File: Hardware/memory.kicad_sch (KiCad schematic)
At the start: 56 parts, among them J2 Micro_SD_Card_Det, U1 STM32MP157FAD1, U3 MT41K256M16TW

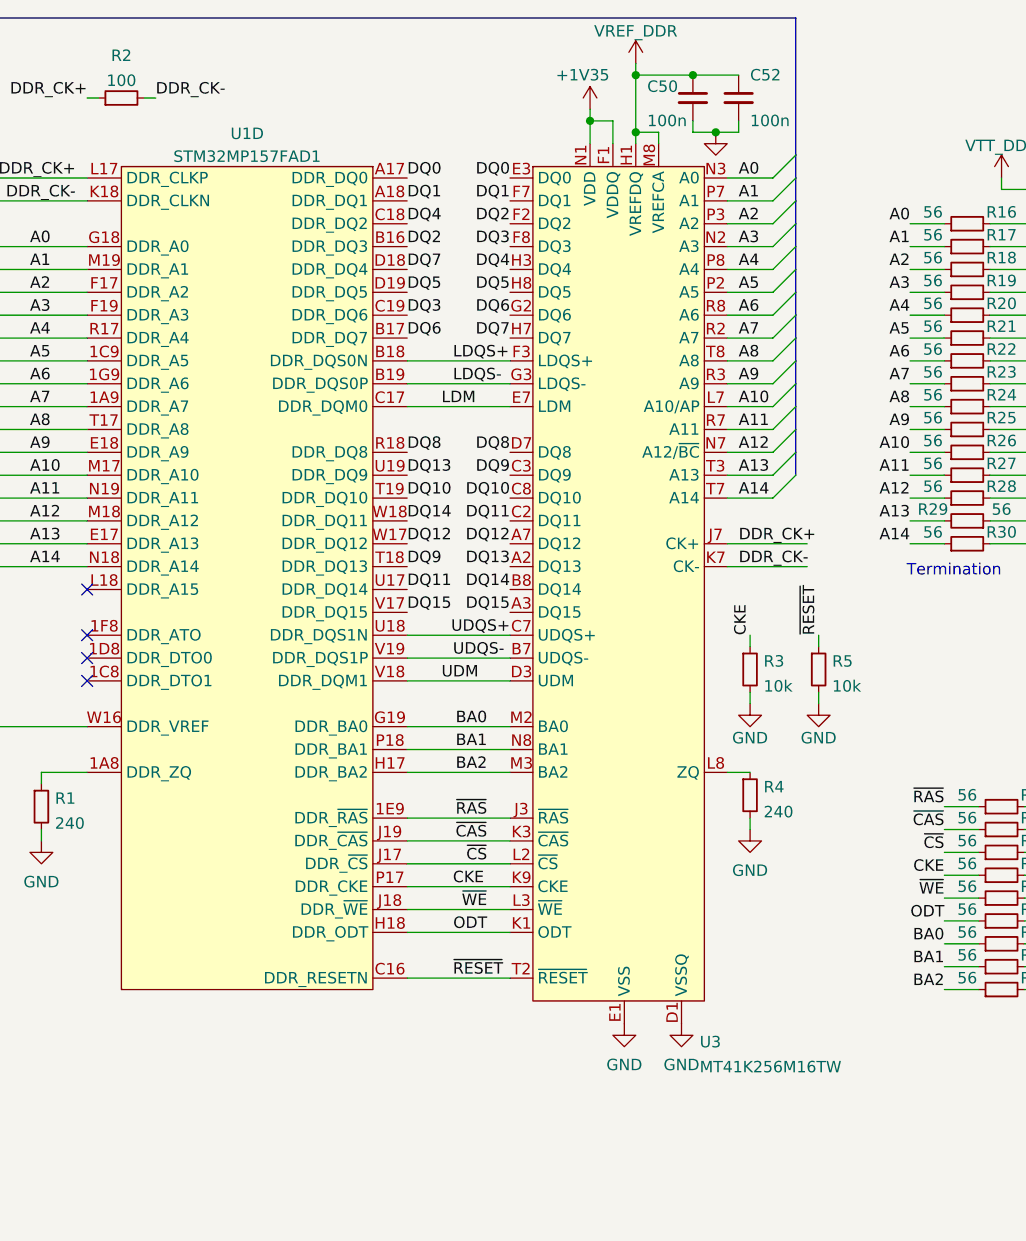
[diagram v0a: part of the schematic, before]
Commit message: Create libraries and move custom symbols to project specific libraries
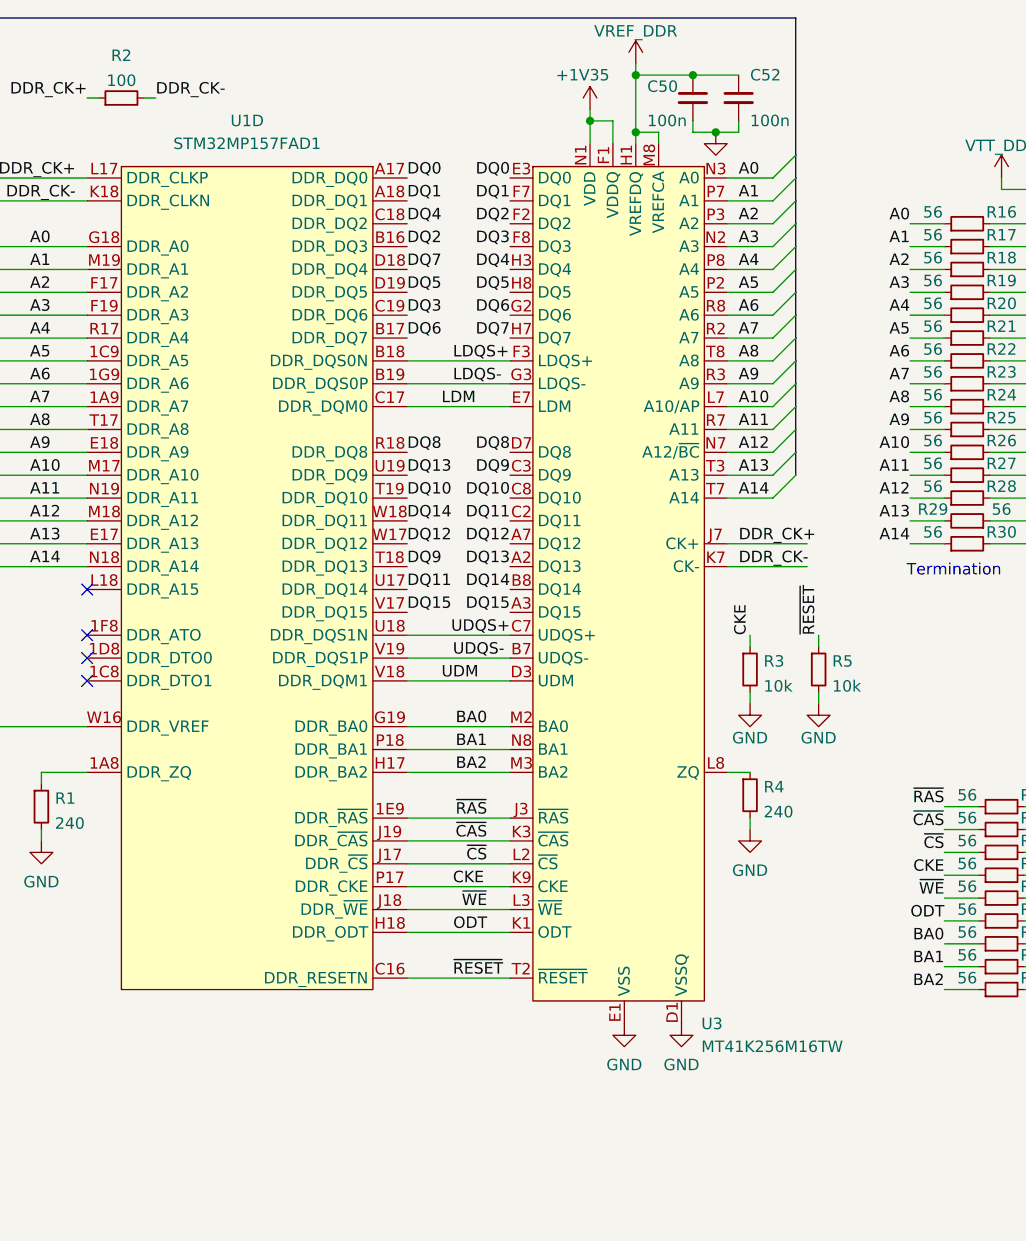
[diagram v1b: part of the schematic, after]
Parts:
- removed U1: STM32MP157FAD1, personal:TFBGA257, symbol Personal:STM32MP157FAD1
- removed U3: MT41K256M16TW, Package_BGA:BGA-96_9.0x13.0mm_Layout2x3x16_P0.8mm, symbol Personal:MT41K256M16TW
- added U1: STM32MP157FAD1, personal:TFBGA257, symbol SimpleSBC:STM32MP157FAD1
- added U3: MT41K256M16TW, Package_BGA:BGA-96_9.0x13.0mm_Layout2x3x16_P0.8mm, symbol SimpleSBC:MT41K256M16TW
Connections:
- net +1V35: now also U3.A1 (VDDQ), U3.A8 (VDDQ), U3.B2 (VDD), U3.C1 (VDDQ), U3.C9 (VDDQ), U3.D2 (VDDQ), U3.D9 (VDD), U3.E9 (VDDQ), U3.F1 (VDDQ), U3.G7 (VDD), U3.H2 (VDDQ), U3.H9 (VDDQ), U3.K2 (VDD), U3.K8 (VDD), U3.N1 (VDD), U3.N9 (VDD), U3.R1 (VDD), U3.R9 (VDD)
- net A0: now also U1.G18 (DDR_A0), U3.N3 (A0)
- net A1: now also U1.M19 (DDR_A1), U3.P7 (A1)
- net A10: now also U1.M17 (DDR_A10), U3.L7 (A10/AP)
- net A11: now also U1.N19 (DDR_A11), U3.R7 (A11)
- net A12: now also U1.M18 (DDR_A12), U3.N7 (A12/~{BC})
- net A13: now also U1.E17 (DDR_A13), U3.T3 (A13)
- net A14: now also U1.N18 (DDR_A14), U3.T7 (A14)
- net A2: now also U1.F17 (DDR_A2), U3.P3 (A2)
- net A3: now also U1.F19 (DDR_A3), U3.N2 (A3)
- net A4: now also U1.R17 (DDR_A4), U3.P8 (A4)
- net A5: now also U1.1C9 (DDR_A5), U3.P2 (A5)
- net A6: now also U1.1G9 (DDR_A6), U3.R8 (A6)
- net A7: now also U1.1A9 (DDR_A7), U3.R2 (A7)
- net A8: now also U1.T17 (DDR_A8), U3.T8 (A8)
- net A9: now also U1.E18 (DDR_A9), U3.R3 (A9)
- net BA0: now also U1.G19 (DDR_BA0), U3.M2 (BA0)
- net BA1: now also U1.P18 (DDR_BA1), U3.N8 (BA1)
- net BA2: now also U1.H17 (DDR_BA2), U3.M3 (BA2)
- net CKE: now also U1.P17 (DDR_CKE), U3.K9 (CKE)
- net DDR_CK+: now also U1.L17 (DDR_CLKP), U3.J7 (CK+)
- net DDR_CK-: now also U1.K18 (DDR_CLKN), U3.K7 (CK-)
- net DQ0: now also U1.A17 (DDR_DQ0), U3.E3 (DQ0)
- net DQ1: now also U1.A18 (DDR_DQ1), U3.F7 (DQ1)
- net DQ10: now also U1.T19 (DDR_DQ10), U3.C8 (DQ10)
- net DQ11: now also U1.U17 (DDR_DQ14), U3.C2 (DQ11)
- net DQ12: now also U1.W17 (DDR_DQ12), U3.A7 (DQ12)
- net DQ13: now also U1.U19 (DDR_DQ9), U3.A2 (DQ13)
- net DQ14: now also U1.W18 (DDR_DQ11), U3.B8 (DQ14)
- net DQ15: now also U1.V17 (DDR_DQ15), U3.A3 (DQ15)
- net DQ2: now also U1.B16 (DDR_DQ3), U3.F2 (DQ2)
- net DQ3: now also U1.C19 (DDR_DQ6), U3.F8 (DQ3)
- net DQ4: now also U1.C18 (DDR_DQ2), U3.H3 (DQ4)
- net DQ5: now also U1.D19 (DDR_DQ5), U3.H8 (DQ5)
- net DQ6: now also U1.B17 (DDR_DQ7), U3.G2 (DQ6)
- net DQ7: now also U1.D18 (DDR_DQ4), U3.H7 (DQ7)
- net DQ8: now also U1.R18 (DDR_DQ8), U3.D7 (DQ8)
- net DQ9: now also U1.T18 (DDR_DQ13), U3.C3 (DQ9)
- net GND: now also U3.A9 (VSS), U3.B1 (VSSQ), U3.B3 (VSS), U3.B9 (VSSQ), U3.D1 (VSSQ), U3.D8 (VSSQ), U3.E1 (VSS), U3.E2 (VSSQ), U3.E8 (VSSQ), U3.F9 (VSSQ), U3.G1 (VSSQ), U3.G8 (VSS), U3.G9 (VSSQ), U3.J2 (VSS), U3.J8 (VSS), U3.M1 (VSS), U3.M9 (VSS), U3.P1 (VSS), U3.P9 (VSS), U3.T1 (VSS), U3.T9 (VSS)
- net LDM: now also U1.C17 (DDR_DQM0), U3.E7 (LDM)
- net LDQS+: now also U1.B18 (DDR_DQS0N), U3.F3 (LDQS+)
- net LDQS-: now also U1.B19 (DDR_DQS0P), U3.G3 (LDQS-)
- net ODT: now also U1.H18 (DDR_ODT), U3.K1 (ODT)
- net UDM: now also U1.V18 (DDR_DQM1), U3.D3 (UDM)
- net UDQS+: now also U1.U18 (DDR_DQS1N), U3.C7 (UDQS+)
- net UDQS-: now also U1.V19 (DDR_DQS1P), U3.B7 (UDQS-)
- net VREF_DDR: now also U1.W16 (DDR_VREF), U3.H1 (VREFDQ), U3.M8 (VREFCA)
- net ~{CAS}: now also U1.J19 (DDR_~{CAS}), U3.K3 (~{CAS})
- net ~{CS}: now also U1.J17 (DDR_~{CS}), U3.L2 (~{CS})
- net ~{RAS}: now also U1.1E9 (DDR_~{RAS}), U3.J3 (~{RAS})
- net ~{RESET}: now also U1.C16 (DDR_RESETN), U3.T2 (~{RESET})
- net ~{WE}: now also U1.J18 (DDR_~{WE}), U3.L3 (~{WE})
- net at R1.1: now also U1.1A8 (DDR_ZQ)
- net at R4.1: now also U3.L8 (ZQ)

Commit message: First Draft schematic (R2)
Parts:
- U1: footprint personal:TFBGA257 -> SimpleSBC:TFBGA257
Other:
- title: (none) -> SimpleSBC Memory
- moved on the sheet: C2, C50, C51, C52, C53, C54, C55, C56, C57, C58, C59, C60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

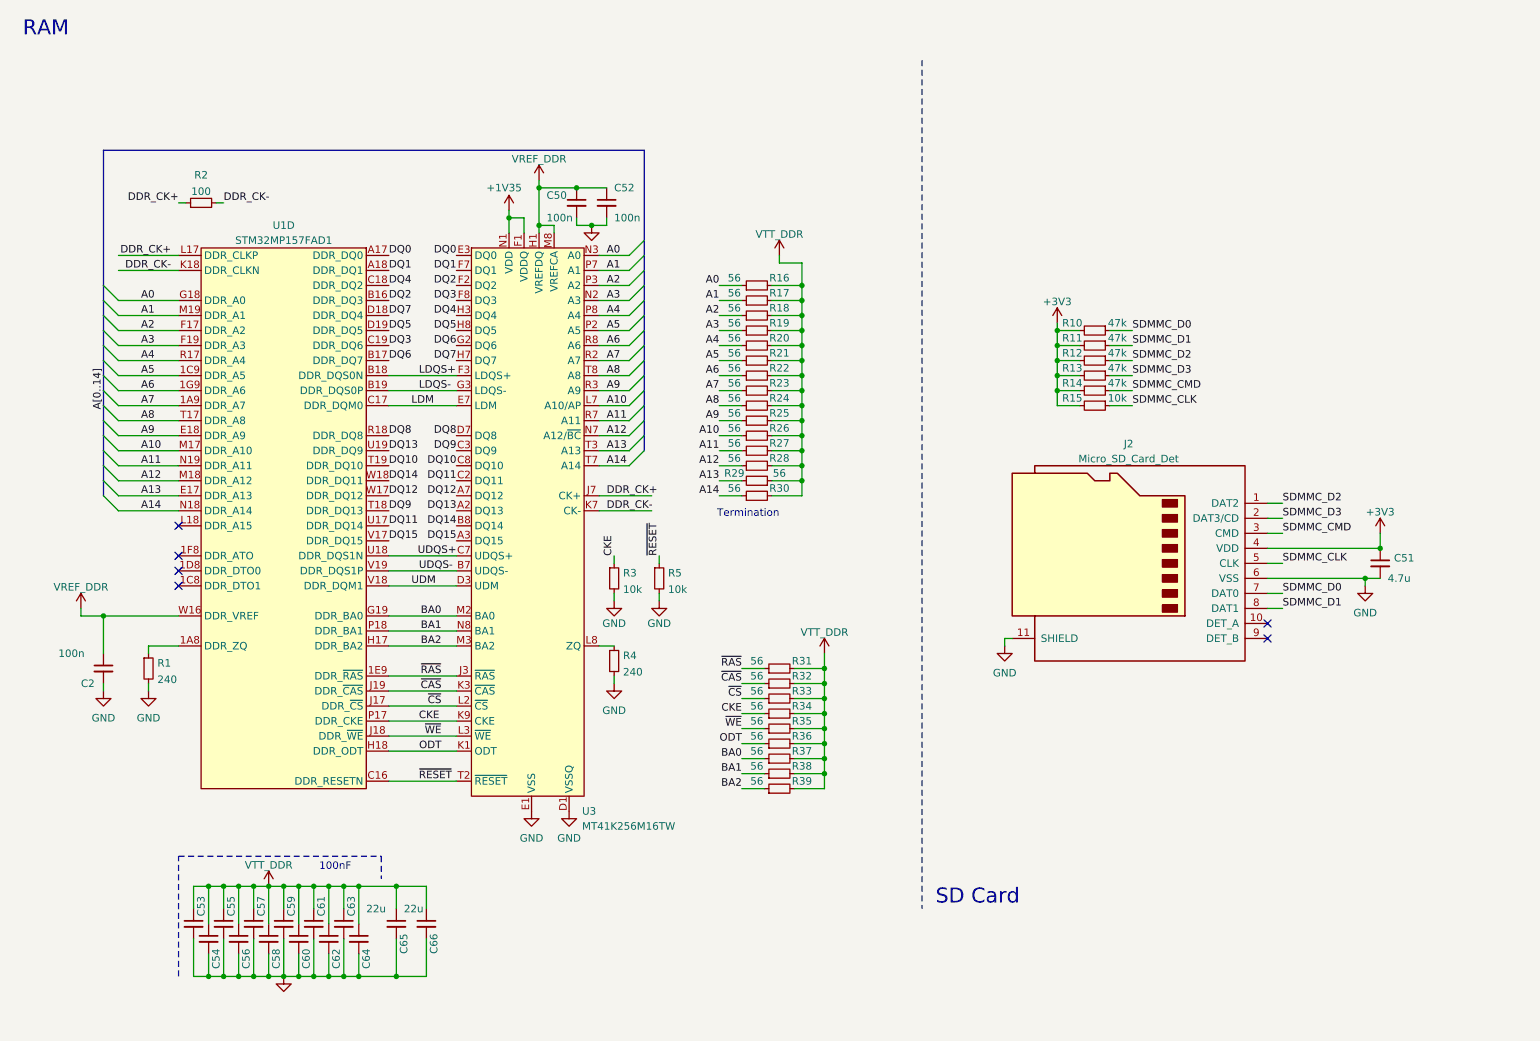
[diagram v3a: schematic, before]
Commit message: Schematic symbol pin type fixes
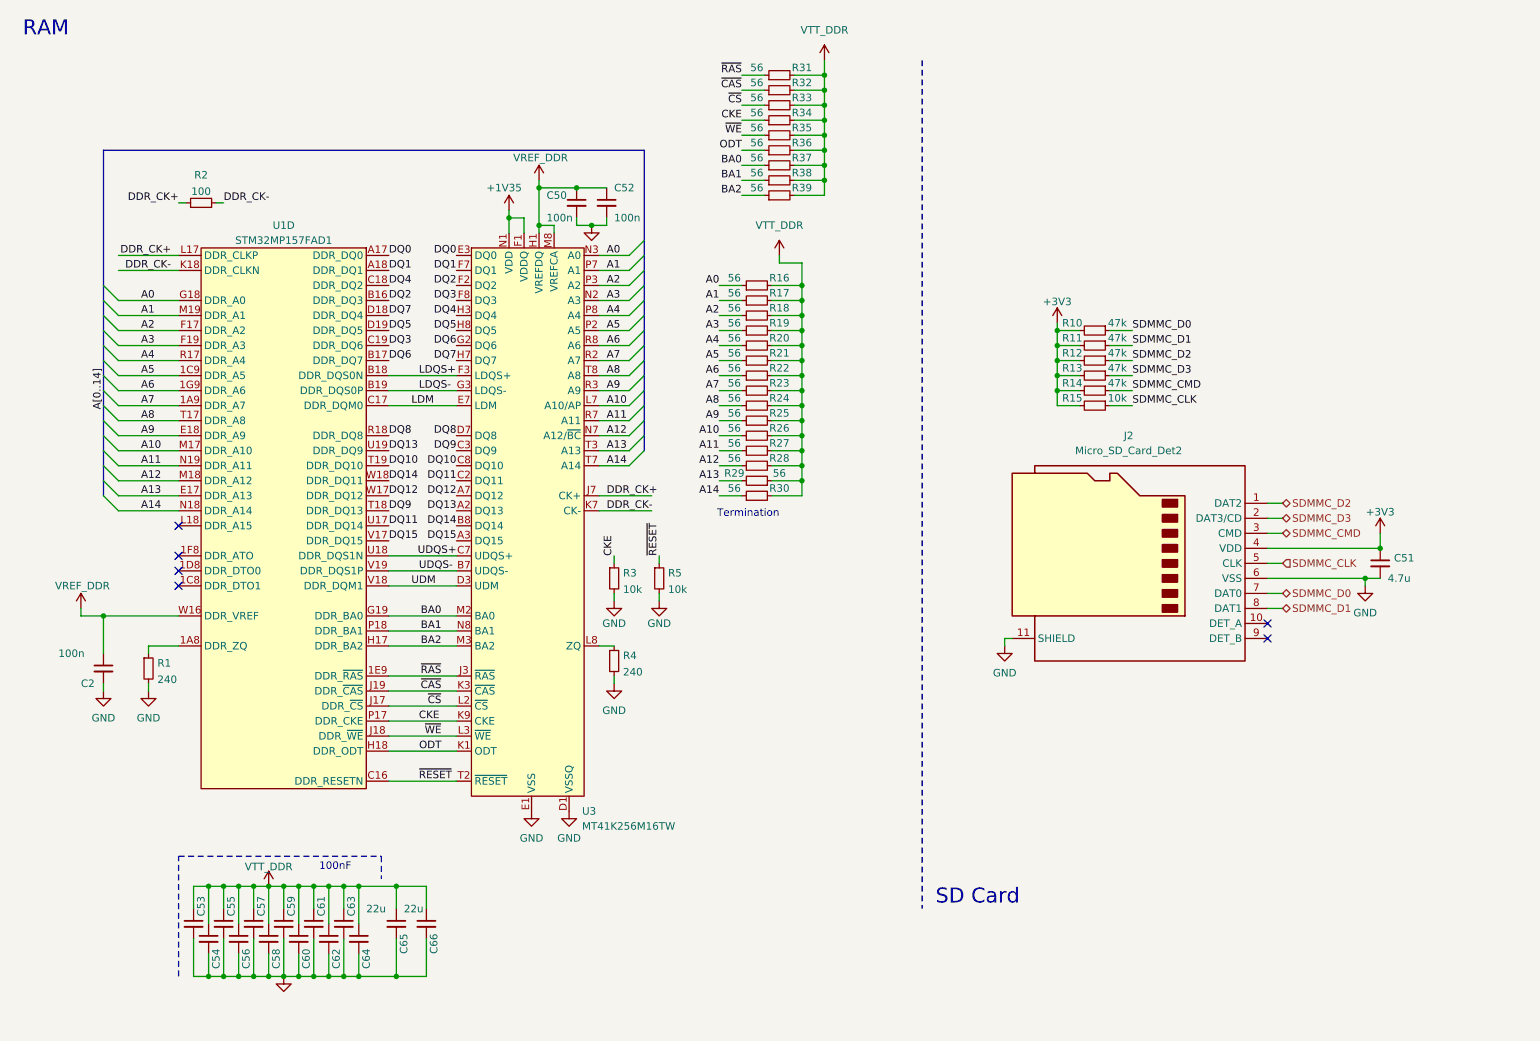
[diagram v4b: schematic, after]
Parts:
- removed J2: Micro_SD_Card_Det, Connector_Card:microSD_HC_Molex_104031-0811, symbol Connector:Micro_SD_Card_Det
- added J2: Micro_SD_Card_Det2, Connector_Card:microSD_HC_Molex_104031-0811, symbol Connector:Micro_SD_Card_Det2
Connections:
- net +3V3: now also J2.4 (VDD)
- net GND: now also J2.11 (SHIELD), J2.6 (VSS)
- net SDMMC_CLK: now also J2.5 (CLK)
- net SDMMC_CMD: now also J2.3 (CMD)
- net SDMMC_D0: now also J2.7 (DAT0)
- net SDMMC_D1: now also J2.8 (DAT1)
- net SDMMC_D2: now also J2.1 (DAT2)
- net SDMMC_D3: now also J2.2 (DAT3/CD)
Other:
- moved on the sheet: R31, R32, R33, R34, R35, R36, R37, R38, R39

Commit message: First pass through ST Design Checklist
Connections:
- net +3V3: no longer C51.1, J2.4 (VDD)
- net LDM: now also U1.V18 (DDR_DQM1); no longer U1.C17 (DDR_DQM0)
- net LDQS+: now also U1.V19 (DDR_DQS1P); no longer U1.B18 (DDR_DQS0N)
- net LDQS-: now also U1.U18 (DDR_DQS1N); no longer U1.B19 (DDR_DQS0P)
- net UDM: now also U1.C17 (DDR_DQM0); no longer U1.V18 (DDR_DQM1)
- net UDQS+: now also U1.B19 (DDR_DQS0P); no longer U1.U18 (DDR_DQS1N)
- net UDQS-: now also U1.B18 (DDR_DQS0N); no longer U1.V19 (DDR_DQS1P)
- new net +3.3VP: C51.1, J2.4 (VDD)
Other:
- note added: "Place after DRAM balls"
- moved on the sheet: C2, R1, R2, U1D

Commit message: First Pass Routing
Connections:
- net +3V3 is gone; now on net +3.3VP: R10.2, R11.2, R12.2, R13.2, R14.2, R15.2

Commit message: ERC/DRC Clean
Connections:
- net LDM: now also U1.C17 (DDR_DQM0); no longer U1.V18 (DDR_DQM1)
- net LDQS+: now also U1.B19 (DDR_DQS0P); no longer U1.V19 (DDR_DQS1P)
- net LDQS-: now also U1.B18 (DDR_DQS0N); no longer U1.U18 (DDR_DQS1N)
- net UDM: now also U1.V18 (DDR_DQM1); no longer U1.C17 (DDR_DQM0)
- net UDQS+: now also U1.V19 (DDR_DQS1P); no longer U1.B19 (DDR_DQS0P)
- net UDQS-: now also U1.U18 (DDR_DQS1N); no longer U1.B18 (DDR_DQS0N)
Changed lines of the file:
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@@
 	(wire
 		(pts
-			(xy 31.75 57.15) (xy 41.91 57.15)
+			(xy 40.64 57.15) (xy 41.91 57.15)
 		)
 		(stroke
@@
 	(wire
 		(pts
-			(xy 115.57 95.25) (xy 124.46 95.25)
+			(xy 115.57 95.25) (xy 116.84 95.25)
 		)
 		(stroke
@@
 	(wire
 		(pts
-			(xy 31.75 54.61) (xy 41.91 54.61)
+			(xy 40.64 54.61) (xy 41.91 54.61)
 		)
 		(stroke
@@
 	(wire
 		(pts
-			(xy 115.57 97.79) (xy 124.46 97.79)
+			(xy 115.57 97.79) (xy 116.84 97.79)
 		)
 		(stroke
@@
 	)
 	(label "UDM"
-		(at 77.47 80.01 0)
+		(at 77.47 110.49 0)
 		(effects
 			(font
@@
 	)
 	(label "LDM"
-		(at 77.47 110.49 0)
+		(at 77.47 80.01 0)
 		(effects
 			(font
@@
 	)
 	(label "LDQS+"
-		(at 77.47 107.95 0)
+		(at 77.47 77.47 0)
 		(effects
 			(font
@@
 	)
 	(label "UDQS-"
-		(at 77.47 74.93 0)
+		(at 77.47 105.41 0)
 		(effects
 			(font
@@
 	)
 	(label "UDQS+"
-		(at 77.47 77.47 0)
+		(at 77.47 107.95 0)
 		(effects
 			(font
@@
 	)
 	(label "LDQS-"
-		(at 77.47 105.41 0)
+		(at 77.47 74.93 0)
 		(effects
 			(font

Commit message: prepare for assembly
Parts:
- C2, C50, C52, C53, C54, C55, C56, C57, C58, C59, C60, C61, C62, C63, C64: JLCPCB Part # (none) -> C1525
- C51: footprint Capacitor_SMD:C_0603_1608Metric -> Capacitor_SMD:C_0402_1005Metric; JLCPCB Part # (none) -> C23733
- C65, C66: JLCPCB Part # (none) -> C45783
- J2: now not fitted
- R1, R4: JLCPCB Part # (none) -> C208835
- R10, R11, R12, R13, R14: JLCPCB Part # (none) -> C25792
- R15, R3, R5: JLCPCB Part # (none) -> C25744
- R16, R17, R18, R19, R20, R21, R22, R23, R24, R25, R26, R27, R28, R29, R30, R31, R32, R33, R34, R35, R36, R37, R38, R39: JLCPCB Part # (none) -> C25127
- R2: JLCPCB Part # (none) -> C25076
- U1: JLCPCB Part # (none) -> C1236719
- U3: JLCPCB Part # (none) -> C253882
